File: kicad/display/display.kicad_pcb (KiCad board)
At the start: 2 copper layers, 190.5 x 38.1 mm, 25 parts, among them J1 Conn. 02x12, P1 10k, P2 10k, P3 10k stereo, P4 10k, T1 2N3904, T2 2N3904, U1 4066N, U2 RC1602A

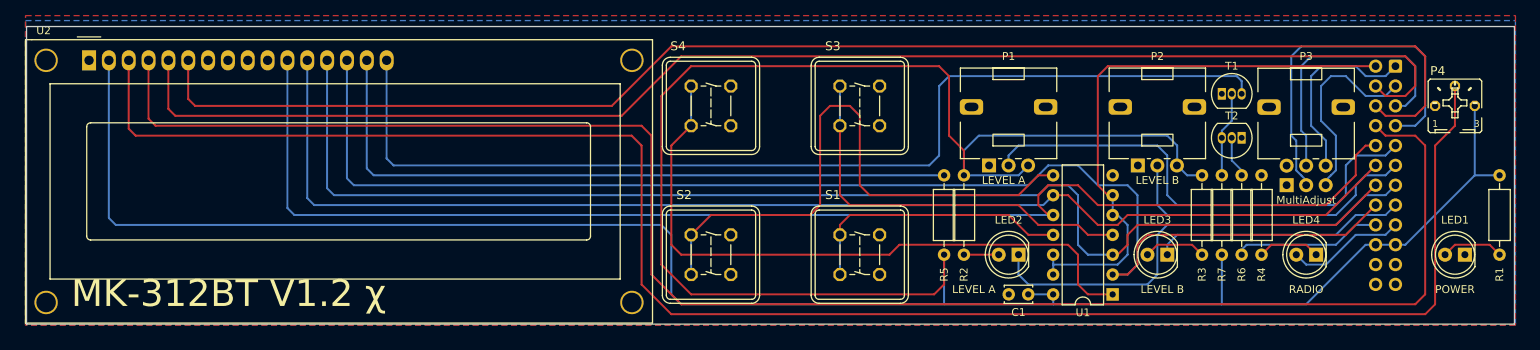
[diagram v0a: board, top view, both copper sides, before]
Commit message: Fixing mounting holes for display print
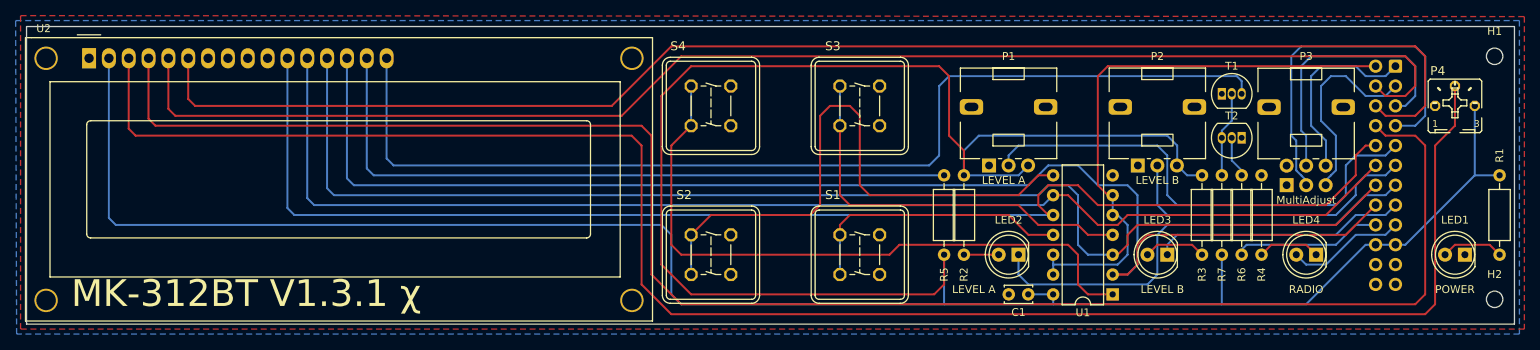
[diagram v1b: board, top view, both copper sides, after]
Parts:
- added H1: MountingHole topright, MountingHole:MountingHole_2.1mm, F.Cu at (238.8, 54.6)
- added H2: MountingHole bottomright, MountingHole:MountingHole_2.1mm, F.Cu at (238.8, 85.7)
- moved U2 0.26 mm to (58.8, 54.9)
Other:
- board text added: "MK-312BT V1.3.1 χ"
- board text removed: "MK-312BT V1.2 χ"
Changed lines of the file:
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@@
   )
   (paper "A4")
+  (title_block
+    (title "MK312BT Display Print")
+    (date "2022-08-01")
+    (rev "1.3.1-Chi")
+  )
   (layers
     (0 "F.Cu" signal)
@@
       (layerselection 0x00010fc_ffffffff)
       (disableapertmacros false)
-      (usegerberextensions false)
+      (usegerberextensions true)
       (usegerberattributes true)
       (usegerberadvancedattributes true)
-      (creategerberjobfile true)
+      (creategerberjobfile false)
       (svguseinch false)
       (svgprecision 6)
@@
       (outputformat 1)
       (mirror false)
-      (drillshape 1)
+      (drillshape 0)
       (scaleselection 1)
-      (outputdirectory "")
+      (outputdirectory "gerber")
     )
   )
@@
     )
   )
+  (footprint "MountingHole:MountingHole_2.1mm" (layer "F.Cu")
+    (at 238.76 54.61)
+    (descr "Mounting Hole 2.1mm, no annular")
+    (tags "mounting hole 2.1mm no annular")
+    (property "Sheetfile" "display.kicad_sch")
+    (property "Sheetname" "")
+    (attr exclude_from_pos_files)
+    (fp_text reference "H1" (at 0 -3.2) (layer "F.SilkS")
+      (effects (font (size 1 1) (thickness 0.15)))
+    )
+    (fp_text value "MountingHole topright" (at 0 3.2) (layer "F.Fab")
+      (effects (font (size 1 1) (thickness 0.15)))
+    )
+    (fp_text user "${REFERENCE}" (at 0 0) (layer "F.Fab")
+      (effects (font (size 1 1) (thickness 0.15)))
+    )
+    (fp_circle (center 0 0) (end 2.1 0) (layer "Cmts.User") (width 0.15) (fill none))
+    (fp_circle (center 0 0) (end 2.35 0) (layer "F.CrtYd") (width 0.05) (fill none))
+    (pad "" np_thru_hole circle (at 0 0) (size 2.1 2.1) (drill 2.1) (layers *.Cu *.Mask))
+  )
   (footprint "Resistor_THT:R_Axial_DIN0207_L6.3mm_D2.5mm_P10.16mm_Horizontal" (layer "F.Cu")
     (at 203.835 69.85 -90)
@@
     (pad "3" thru_hole circle (at 0 5 90) (size 1.8 1.8) (drill 1) (layers *.Cu *.Mask)
       (net 30 "+5V") (pinfunction "3") (pintype "passive"))
-    (pad "MP" thru_hole roundrect (at 7.5 7.25 90) (size 2 3) (drill oval 1.1 1.8) (layers *.Cu *.Mask) (roundrect_rratio 0.25))
-    (pad "MP" thru_hole roundrect (at 7.5 -2.25 90) (size 2 3) (drill oval 1.1 1.8) (layers *.Cu *.Mask) (roundrect_rratio 0.25))
+    (pad "MP" thru_hole roundrect (at 7.500011 7.249998 90) (size 2 2.999999) (drill oval 1.1 1.8) (layers *.Cu *.Mask) (roundrect_rratio 0.25))
+    (pad "MP" thru_hole roundrect (at 7.500011 -2.250008 90) (size 2 2.999999) (drill oval 1.1 1.8) (layers *.Cu *.Mask) (roundrect_rratio 0.25))
     (zone (net 0) (net_name "") (layer "F.Cu") (name "Copper Keep Out") (hatch full 0.508)
       (connect_pads (clearance 0))
@@
     (property "Sheetname" "")
     (attr through_hole)
-    (fp_text reference "R1" (at -2.54 0 90) (layer "F.SilkS")
+    (fp_text reference "R1" (at 12.7 0 90) (layer "F.SilkS")
       (effects (font (size 1 1) (thickness 0.15)))
     )
@@
       (rotate (xyz 0 0 0))
     )
+  )
+  (footprint "MountingHole:MountingHole_2.1mm" (layer "F.Cu")
+    (at 238.76 85.725)
+    (descr "Mounting Hole 2.1mm, no annular")
+    (tags "mounting hole 2.1mm no annular")
+    (property "Sheetfile" "display.kicad_sch")
+    (property "Sheetname" "")
+    (attr exclude_from_pos_files)
+    (fp_text reference "H2" (at 0 -3.2) (layer "F.SilkS")
+      (effects (font (size 1 1) (thickness 0.15)))
+    )
+    (fp_text value "MountingHole bottomright" (at 0 3.2) (layer "F.Fab")
+      (effects (font (size 1 1) (thickness 0.15)))
+    )
+    (fp_text user "${REFERENCE}" (at 0 0) (layer "F.Fab")
+      (effects (font (size 1 1) (thickness 0.15)))
+    )
+    (fp_circle (center 0 0) (end 2.1 0) (layer "Cmts.User") (width 0.15) (fill none))
+    (fp_circle (center 0 0) (end 2.35 0) (layer "F.CrtYd") (width 0.05) (fill none))
+    (pad "" np_thru_hole circle (at 0 0) (size 2.1 2.1) (drill 2.1) (layers *.Cu *.Mask))
   )
   (footprint "Potentiometer_THT:Potentiometer_Alps_RK09L_Double_Vertical" (layer "F.Cu")
@@
     (pad "6" thru_hole circle (at 2.5 5 90) (size 1.8 1.8) (drill 1) (layers *.Cu *.Mask)
       (net 1 "Net-(J1-Pad1)") (pinfunction "6") (pintype "passive"))
-    (pad "MP" thru_hole roundrect (at 10 -2.25 90) (size 2 3) (drill oval 1.1 1.8) (layers *.Cu *.Mask) (roundrect_rratio 0.25))
-    (pad "MP" thru_hole roundrect (at 10 7.25 90) (size 2 3) (drill oval 1.1 1.8) (layers *.Cu *.Mask) (roundrect_rratio 0.25))
+    (pad "MP" thru_hole roundrect (at 10.000005 -2.250008 90) (size 2 2.999999) (drill oval 1.1 1.8) (layers *.Cu *.Mask) (roundrect_rratio 0.25))
+    (pad "MP" thru_hole roundrect (at 10.000005 7.249998 90) (size 2 2.999999) (drill oval 1.1 1.8) (layers *.Cu *.Mask) (roundrect_rratio 0.25))
     (zone (net 0) (net_name "") (layer "F.Cu") (name "Copper Keep Out") (hatch full 0.508)
       (connect_pads (clearance 0))
@@
     (pad "3" thru_hole circle (at 0 5 90) (size 1.8 1.8) (drill 1) (layers *.Cu *.Mask)
       (net 30 "+5V") (pinfunction "3") (pintype "passive"))
-    (pad "MP" thru_hole roundrect (at 7.5 7.25 90) (size 2 3) (drill oval 1.1 1.8) (layers *.Cu *.Mask) (roundrect_rratio 0.25))
-    (pad "MP" thru_hole roundrect (at 7.5 -2.25 90) (size 2 3) (drill oval 1.1 1.8) (layers *.Cu *.Mask) (roundrect_rratio 0.25))
+    (pad "MP" thru_hole roundrect (at 7.500011 7.249998 90) (size 2 2.999999) (drill oval 1.1 1.8) (layers *.Cu *.Mask) (roundrect_rratio 0.25))
+    (pad "MP" thru_hole roundrect (at 7.500011 -2.250008 90) (size 2 2.999999) (drill oval 1.1 1.8) (layers *.Cu *.Mask) (roundrect_rratio 0.25))
     (zone (net 0) (net_name "") (layer "F.Cu") (name "Copper Keep Out") (hatch full 0.508)
       (connect_pads (clearance 0))
@@
   )
   (footprint "Display:WC1602A" (layer "F.Cu")
-    (at 58.805 55.1275)
+    (at 58.804988 54.864)
     (descr "LCD 16x2 http://www.wincomlcd.com/pdf/WC1602A-SFYLYHTC06.pdf")
     (tags "LCD 16x2 Alphanumeric 16pin")
@@
     (fp_line (start 5.72 -33.04) (end -3.18 -33.04) (layer "B.Fab") (width 0.1))
     (fp_line (start -3.18 -11.92) (end -1.98 -11.92) (layer "B.Fab") (width 0.1))
-    (pad "1" thru_hole roundrect (at 0 0 180) (size 1.7 1.7) (drill 1) (layers *.Cu *.Mask) (roundrect_rratio 0.147059)
+    (pad "1" thru_hole roundrect (at 0 0 180) (size 1.7 1.7) (drill 1) (layers *.Cu *.Mask) (roundrect_rratio 0.1470588235)
       (net 1 "Net-(J1-Pad1)") (pinfunction "Pin_1") (pintype "passive"))
     (pad "2" thru_hole circle (at 2.54 0 180) (size 1.7 1.7) (drill 1) (layers *.Cu *.Mask)
@@
   (gr_line (start 241.3 50.8) (end 50.8 50.8) (layer "Edge.Cuts") (width 0.05))
   (gr_line (start 241.3 88.9) (end 241.3 50.8) (layer "Edge.Cuts") (width 0.05))
-  (gr_text "MK-312BT V1.2 χ" (at 56.515 86.995) (layer "F.SilkS")
+  (gr_text "MK-312BT V1.3.1 χ" (at 56.515 86.995) (layer "F.SilkS")
     (effects (font (size 3.429 3.429) (thickness 0.381)) (justify left bottom))
   )
@@
     (polygon
       (pts
-        (xy 241.427 89.027)
-        (xy 50.673 89.027)
-        (xy 50.673 49.403)
-        (xy 241.427 49.403)
+        (xy 242.57 89.535)
+        (xy 50.038 89.535)
+        (xy 50.038 49.403)
+        (xy 242.57 49.53)
       )
     )
@@
     (polygon
       (pts
-        (xy 241.427 89.027)
-        (xy 50.673 89.027)
-        (xy 50.673 50.038)
-        (xy 241.427 50.038)
+        (xy 241.935 90.17)
+        (xy 49.53 90.17)
+        (xy 49.403 50.038)
+        (xy 241.935 50.038)
       )
     )

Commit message: Display print is now on parity with V1.4, but has been re-routed. U3 has also been rotated 180 degrees. Some components have been moved to other places as well
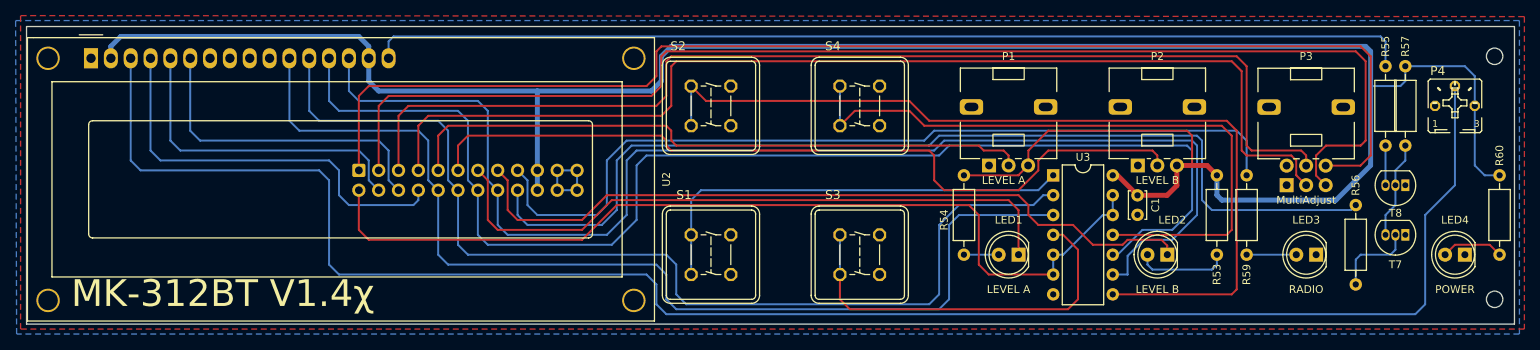
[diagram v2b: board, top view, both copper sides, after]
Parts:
- R55: renamed from R5; value 47 -> 100
- moved J10 133.4 mm to (93.3, 69.2), turned to -90 degrees
- moved R55 61.5 mm to (224.8, 55.9), turned to -90 degrees
- moved T8 26.2 mm to (227.3, 71.1), turned to 180 degrees
- moved T7 24.4 mm to (227.3, 77.5)
- moved R57 23.8 mm to (227.3, 66.0), turned to 90 degrees
- moved C1 18.9 mm to (193.0, 72.4), turned to -90 degrees
- moved U3 17.0 mm to (182.2, 69.8), turned to 0 degrees
- moved R56 15.9 mm to (221.0, 73.7), turned to -90 degrees
- moved R59 10.3 mm to (207.0, 80.0), turned to 90 degrees
- moved R53 1.91 mm to (203.2, 69.8)
- moved U2 0.25 mm to (59.1, 54.9)
- renumbered J1 to J10, LED2 to LED1, LED3 to LED2, LED4 to LED3, LED1 to LED4, R3 to R53, R2 to R54, R7 to R56, R6 to R57, R4 to R59, R1 to R60, S2 to S1, S4 to S2, S1 to S3, S3 to S4, T2 to T7, T1 to T8, U1 to U3
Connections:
- J10 pad 10: Net-(J1-Pad10) -> Net-(J10-Pad10)
- J10 pad 12: Net-(J1-Pad12) -> Net-(J10-Pad12)
- J10 pad 14: Net-(J1-Pad14) -> Net-(J10-Pad14)
- J10 pad 16: Net-(J1-Pad16) -> Net-(J10-Pad16)
- J10 pad 17: Net-(J1-Pad17) -> Net-(J10-Pad17)
- LED3 pad 1: Net-(LED4-Pad1) -> GND
- LED3 pad 2: Net-(J1-Pad17) -> Net-(LED3-Pad2)
- P3 pad MP: (no net) -> GND
- R55 pad 1: +5V -> Net-(R55-Pad1)
- R55 pad 2: Net-(R5-Pad2) -> Net-(R55-Pad2)
- R59 pad 1: GND -> Net-(LED3-Pad2)
- R59 pad 2: Net-(LED4-Pad1) -> Net-(J10-Pad17)
- S1 pad 1: Net-(S2-Pad1) -> Net-(S1-Pad1)
- S1 pad 2: Net-(S2-Pad1) -> Net-(S1-Pad1)
- S2 pad 1: Net-(S4-Pad1) -> Net-(S2-Pad1)
- S2 pad 2: Net-(S4-Pad1) -> Net-(S2-Pad1)
- S3 pad 1: Net-(S1-Pad1) -> Net-(U3-Pad4)
- S3 pad 2: Net-(S1-Pad1) -> Net-(U3-Pad4)
- S4 pad 1: Net-(S3-Pad1) -> Net-(S4-Pad1)
- S4 pad 2: Net-(S3-Pad1) -> Net-(S4-Pad1)
- T8 pad 3: Net-(T1-Pad3) -> Net-(R55-Pad2)
- U2 pad 11: Net-(J1-Pad10) -> Net-(J10-Pad10)
- U2 pad 12: Net-(J1-Pad12) -> Net-(J10-Pad12)
- U2 pad 13: Net-(J1-Pad14) -> Net-(J10-Pad14)
- U2 pad 14: Net-(J1-Pad16) -> Net-(J10-Pad16)
- U2 pad 15: Net-(R5-Pad2) -> +5V
- U2 pad 16: Net-(T1-Pad3) -> Net-(R55-Pad1)
- U3 pad 1: Net-(S4-Pad1) -> Net-(S1-Pad1)
- U3 pad 10: Net-(J1-Pad10) -> Net-(J10-Pad14)
- U3 pad 11: Net-(S1-Pad1) -> Net-(S4-Pad1)
- U3 pad 2: Net-(J1-Pad16) -> Net-(J10-Pad12)
- U3 pad 3: Net-(J1-Pad14) -> Net-(J10-Pad10)
- U3 pad 4: Net-(S3-Pad1) -> Net-(U3-Pad4)
- U3 pad 9: Net-(J1-Pad12) -> Net-(J10-Pad16)
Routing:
- net Net-(J1-Pad16): track 171.1 -> 0.00 mm
- net Net-(J1-Pad10): track 170.1 -> 0.00 mm
- net Net-(J10-Pad8): track 218.5 -> 52.4 mm
- net Net-(J1-Pad14): track 163.0 -> 0.00 mm
- net Net-(J10-Pad16): track 0.00 -> 161.8 mm
- net Net-(J10-Pad14): track 0.00 -> 160.5 mm
- net Net-(J1-Pad12): track 160.4 -> 0.00 mm
- net Net-(J10-Pad6): track 181.4 -> 41.3 mm
- net Net-(J10-Pad1): track 23.9 -> 163.1 mm
- net Net-(J10-Pad4): track 178.9 -> 41.3 mm
- net Net-(J10-Pad3): track 25.0 -> 161.9 mm
- net Net-(J10-Pad10): track 0.00 -> 136.0 mm
- net Net-(T1-Pad3): track 134.2 -> 0.00 mm
- net Net-(R55-Pad1): track 0.00 -> 133.5 mm
- net Net-(J10-Pad12): track 0.00 -> 133.3 mm
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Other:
- board text added: "MK-312BT V1.4χ"
- board text removed: "MK-312BT V1.3.1 χ"

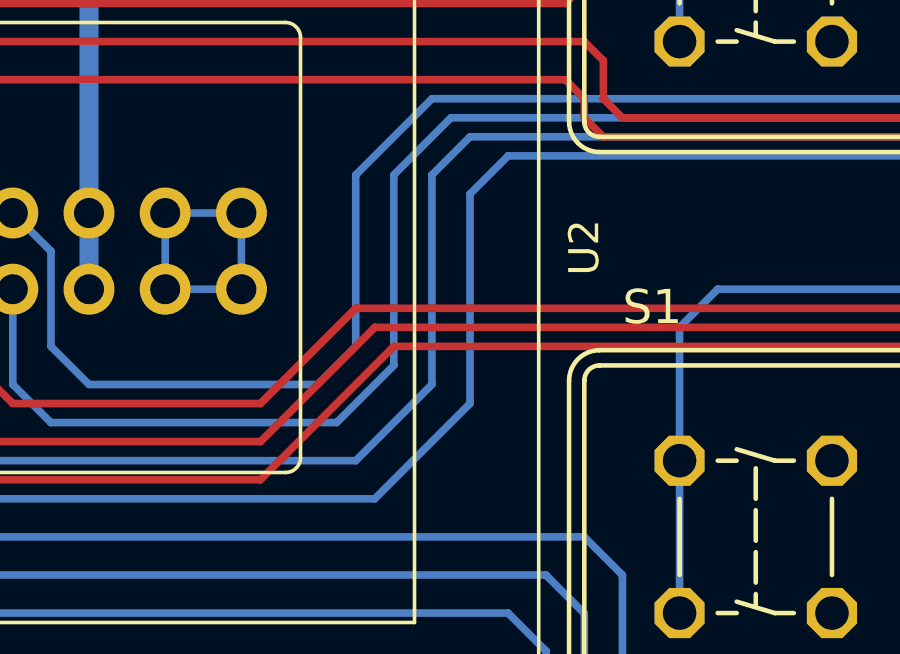
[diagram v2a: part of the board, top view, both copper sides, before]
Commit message: Brought component numbers back in line with the original schematics
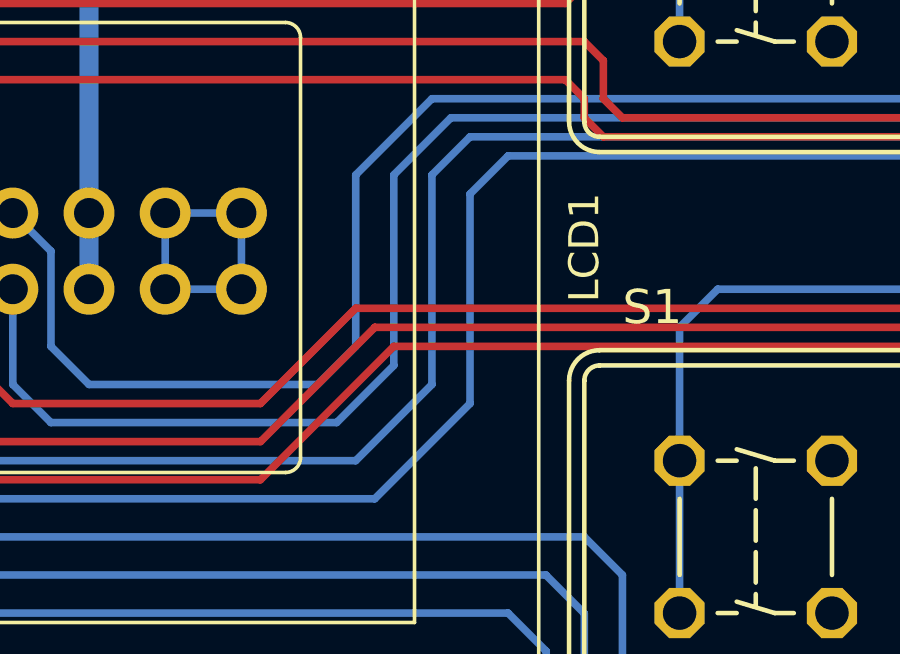
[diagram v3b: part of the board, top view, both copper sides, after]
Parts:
- LED3, LED4: value 5mm, red -> 5 mm, red
- renumbered U2 to LCD1
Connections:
- P3 pad MP: GND -> (no net)
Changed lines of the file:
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@@
   (net 30 "Net-(R55-Pad1)")
   (net 31 "Net-(LED3-Pad2)")
-  (net 32 "Net-(U3-Pad6)")
-  (net 33 "Net-(U3-Pad4)")
+  (net 32 "Net-(J10-Pad2)")
+  (net 33 "Net-(S3-Pad1)")
   (footprint "LED_THT:LED_D5.0mm" (layer "F.Cu")
     (at 234.955004 80.01 180)
@@
       (effects (font (size 1 1) (thickness 0.15)))
     )
-    (fp_text value "5mm, red" (at 1.27 3.96) (layer "F.Fab")
+    (fp_text value "5 mm, red" (at 1.27 3.96) (layer "F.Fab")
       (effects (font (size 1 1) (thickness 0.15)))
     )
@@
       (net 10 "Net-(J10-Pad10)") (pintype "passive"))
     (pad "4" thru_hole oval (at 0 7.62) (size 1.6 1.6) (drill 0.8) (layers *.Cu *.Mask)
-      (net 33 "Net-(U3-Pad4)") (pintype "passive"))
+      (net 33 "Net-(S3-Pad1)") (pintype "passive"))
     (pad "5" thru_hole oval (at 0 10.16) (size 1.6 1.6) (drill 0.8) (layers *.Cu *.Mask)
-      (net 32 "Net-(U3-Pad6)") (pintype "input"))
+      (net 32 "Net-(J10-Pad2)") (pintype "input"))
     (pad "6" thru_hole oval (at 0 12.7) (size 1.6 1.6) (drill 0.8) (layers *.Cu *.Mask)
-      (net 32 "Net-(U3-Pad6)") (pintype "input"))
+      (net 32 "Net-(J10-Pad2)") (pintype "input"))
     (pad "7" thru_hole oval (at 0 15.24) (size 1.6 1.6) (drill 0.8) (layers *.Cu *.Mask)
       (net 2 "GND") (pinfunction "VSS") (pintype "power_in"))
@@
       (net 29 "Net-(S4-Pad1)") (pintype "passive"))
     (pad "12" thru_hole oval (at 7.62 5.08) (size 1.6 1.6) (drill 0.8) (layers *.Cu *.Mask)
-      (net 32 "Net-(U3-Pad6)") (pintype "input"))
+      (net 32 "Net-(J10-Pad2)") (pintype "input"))
     (pad "13" thru_hole oval (at 7.62 2.54) (size 1.6 1.6) (drill 0.8) (layers *.Cu *.Mask)
-      (net 32 "Net-(U3-Pad6)") (pintype "input"))
+      (net 32 "Net-(J10-Pad2)") (pintype "input"))
     (pad "14" thru_hole oval (at 7.62 0) (size 1.6 1.6) (drill 0.8) (layers *.Cu *.Mask)
       (net 27 "+5V") (pinfunction "VDD") (pintype "power_in"))
@@
     (pad "1" thru_hole roundrect (at -2.54 -2.54 90) (size 1.6764 1.6764) (drill 1.1176) (layers *.Cu *.Mask) (roundrect_rratio 0.25)
       (chamfer_ratio 0.2928932188) (chamfer top_left top_right bottom_left bottom_right)
-      (net 33 "Net-(U3-Pad4)") (pinfunction "S") (pintype "passive") (solder_mask_margin 0.1016))
+      (net 33 "Net-(S3-Pad1)") (pinfunction "S") (pintype "passive") (solder_mask_margin 0.1016))
     (pad "2" thru_hole roundrect (at 2.54 -2.54 90) (size 1.6764 1.6764) (drill 1.1176) (layers *.Cu *.Mask) (roundrect_rratio 0.25)
       (chamfer_ratio 0.2928932188) (chamfer top_left top_right bottom_left bottom_right)
-      (net 33 "Net-(U3-Pad4)") (pinfunction "S@1") (pintype "passive") (solder_mask_margin 0.1016))
+      (net 33 "Net-(S3-Pad1)") (pinfunction "S@1") (pintype "passive") (solder_mask_margin 0.1016))
     (pad "3" thru_hole roundrect (at 2.54 2.54 90) (size 1.6764 1.6764) (drill 1.1176) (layers *.Cu *.Mask) (roundrect_rratio 0.25)
       (chamfer_ratio 0.2928932188) (chamfer top_left top_right bottom_left bottom_right)
@@
     (pad "6" thru_hole circle (at 2.5 5 90) (size 1.8 1.8) (drill 1) (layers *.Cu *.Mask)
       (net 1 "Net-(J10-Pad1)") (pinfunction "6") (pintype "passive"))
-    (pad "MP" thru_hole roundrect (at 10.000005 -2.250008 90) (size 2 2.999999) (drill oval 1.1 1.8) (layers *.Cu *.Mask) (roundrect_rratio 0.25)
-      (net 2 "GND"))
-    (pad "MP" thru_hole roundrect (at 10.000005 7.249998 90) (size 2 2.999999) (drill oval 1.1 1.8) (layers *.Cu *.Mask) (roundrect_rratio 0.25)
-      (net 2 "GND"))
+    (pad "MP" thru_hole roundrect (at 10.000005 -2.250008 90) (size 2 2.999999) (drill oval 1.1 1.8) (layers *.Cu *.Mask) (roundrect_rratio 0.25))
+    (pad "MP" thru_hole roundrect (at 10.000005 7.249998 90) (size 2 2.999999) (drill oval 1.1 1.8) (layers *.Cu *.Mask) (roundrect_rratio 0.25))
     (zone (net 0) (net_name "") (layer "F.Cu") (name "Copper Keep Out") (hatch full 0.508)
       (connect_pads (clearance 0))
@@
     (property "Sheetname" "")
     (attr through_hole)
-    (fp_text reference "U2" (at 73.66 15.5 90) (layer "F.SilkS")
+    (fp_text reference "LCD1" (at 73.66 15.5 90) (layer "F.SilkS")
       (effects (font (size 1 1) (thickness 0.15)))
     )
@@
     (fp_arc (start -0.29972 8.49884) (mid -0.153162 8.145018) (end 0.20066 7.99846) (layer "F.SilkS") (width 0.12))
     (fp_arc (start 63.7 8) (mid 64.053553 8.146447) (end 64.2 8.5) (layer "F.SilkS") (width 0.12))
-    (fp_arc (start 64.20104 22.49932) (mid 64.054479 22.85315) (end 63.70066 22.9997) (layer "F.SilkS") (width 0.12))
+    (fp_arc (start 64.20104 22.49932) (mid 64.054473 22.853115) (end 63.70066 22.9997) (layer "F.SilkS") (width 0.12))
     (fp_arc (start 0.20066 22.9997) (mid -0.153162 22.853142) (end -0.29972 22.49932) (layer "F.SilkS") (width 0.12))
     (fp_line (start -8.25 -2.75) (end 72.25 -2.75) (layer "F.CrtYd") (width 0.05))
@@
       (effects (font (size 1 1) (thickness 0.15)))
     )
-    (fp_text value "5mm, red" (at 1.27 3.96) (layer "F.Fab")
+    (fp_text value "5 mm, red" (at 1.27 3.96) (layer "F.Fab")
       (effects (font (size 1 1) (thickness 0.15)))
     )
@@
       (net 1 "Net-(J10-Pad1)") (pinfunction "Pin_1") (pintype "passive"))
     (pad "2" thru_hole circle (at 2.54 0 270) (size 1.7 1.7) (drill 1) (layers *.Cu *.Mask)
-      (net 32 "Net-(U3-Pad6)") (pinfunction "Pin_2") (pintype "passive"))
+      (net 32 "Net-(J10-Pad2)") (pinfunction "Pin_2") (pintype "passive"))
     (pad "3" thru_hole circle (at 0 -2.54 270) (size 1.7 1.7) (drill 1) (layers *.Cu *.Mask)
       (net 3 "Net-(J10-Pad3)") (pinfunction "Pin_3") (pintype "passive"))
